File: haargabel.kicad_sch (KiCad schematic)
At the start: 42 parts, among them J1 USB_B_Micro, J2 Conn_01x03, J3 SWD, SW1 SKRKAEE020, SW2 SKRKAEE020, U1 MCP73831-2-OT, U2 ATSAMD21G18A-M, U3 TPS22929D, U4 TPS79330-EP, U5 MPU-6050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

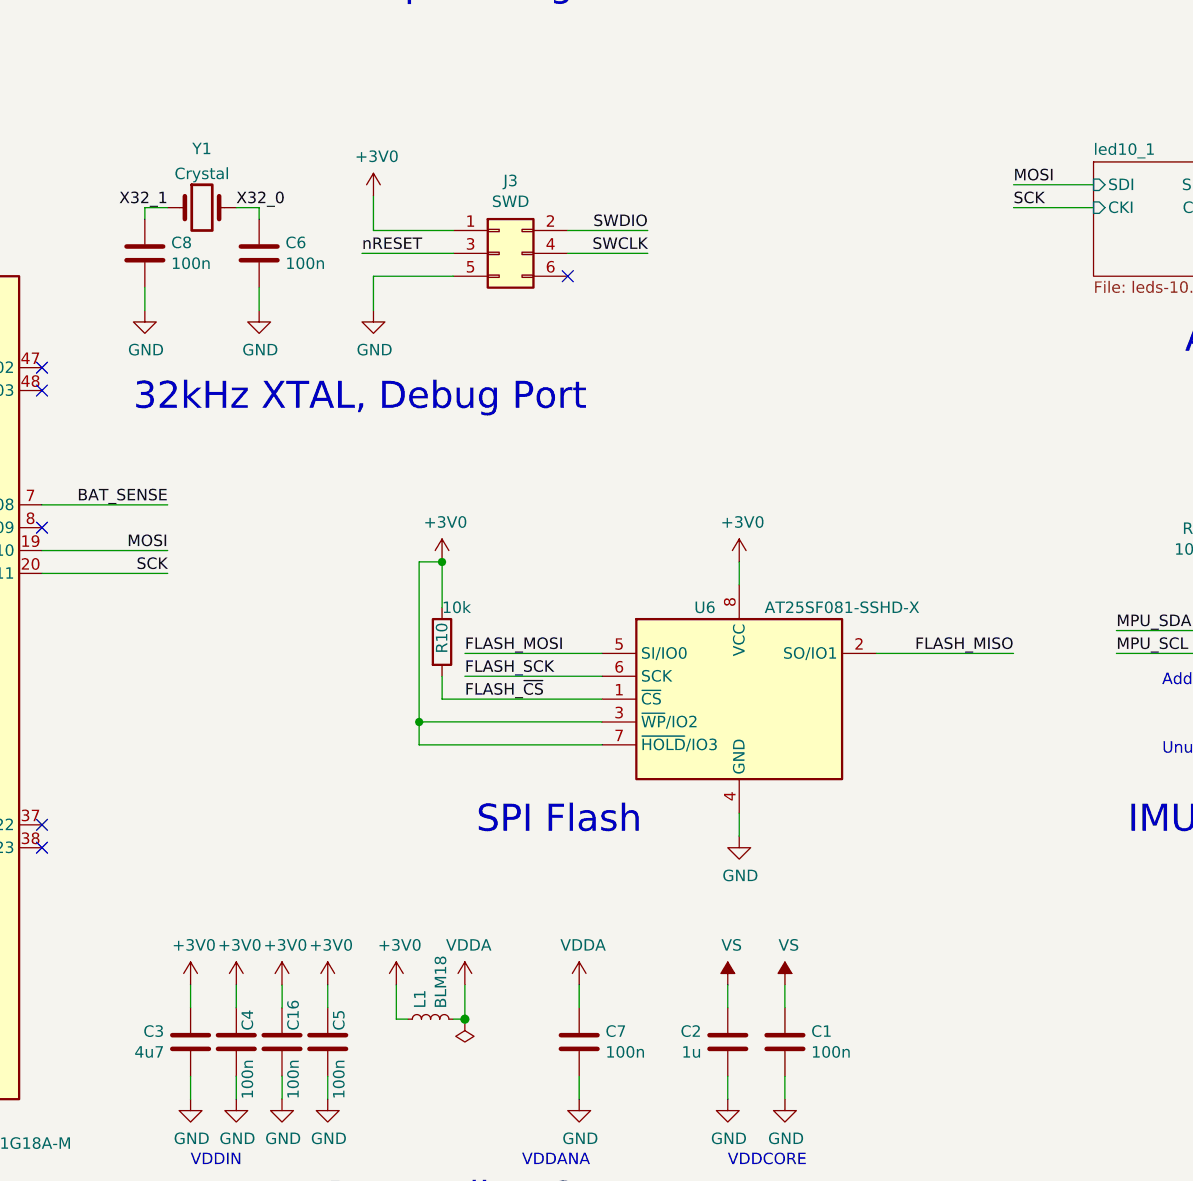
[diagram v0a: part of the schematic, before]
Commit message: Convert to KiCad7, add iBOM
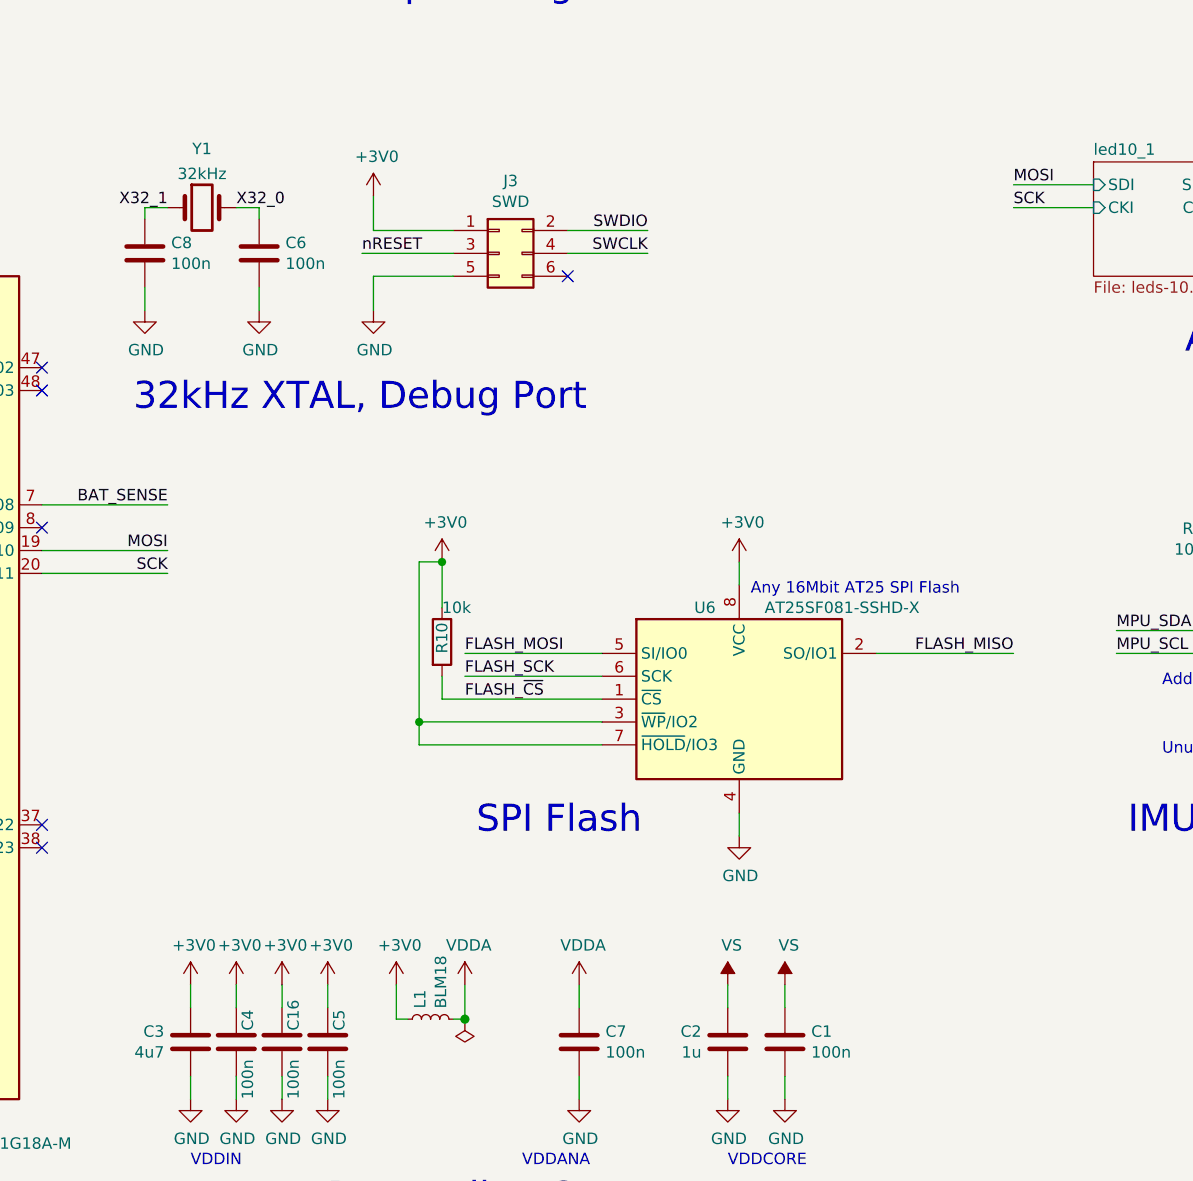
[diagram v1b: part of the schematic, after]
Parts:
- Y1: value Crystal -> 32kHz
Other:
- note added: "Any 16Mbit AT25 SPI Flash"

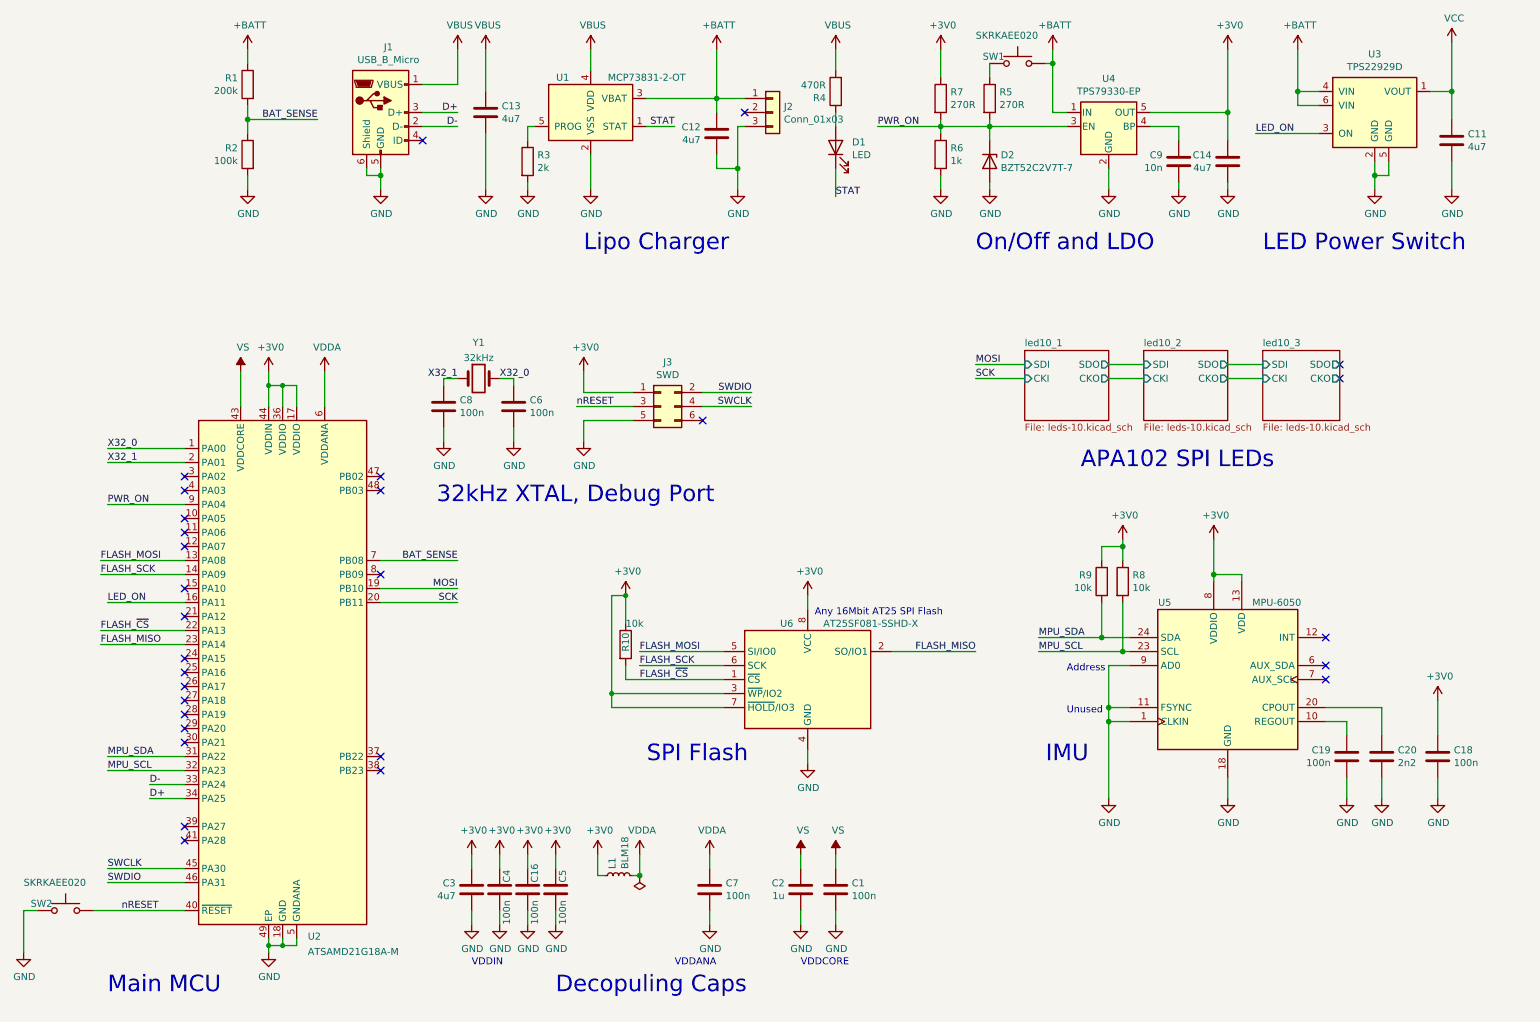
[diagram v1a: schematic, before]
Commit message: Simplify component values
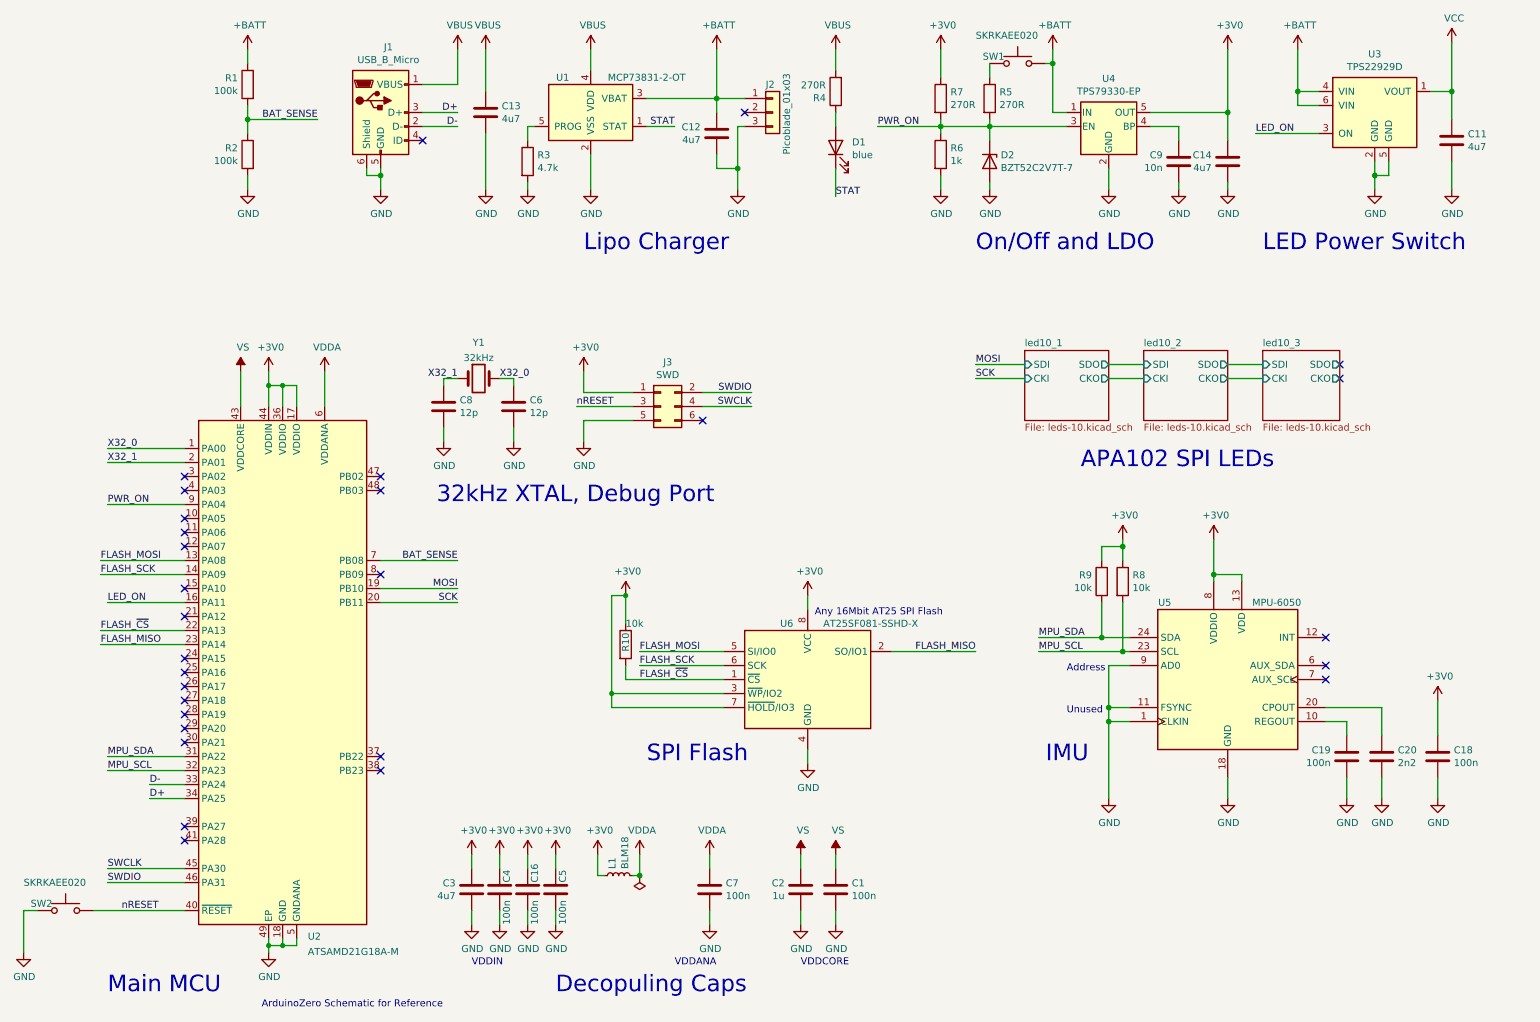
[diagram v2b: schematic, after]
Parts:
- C6, C8: value 100n -> 12p
- D1: value LED -> blue
- J2: value Conn_01x03 -> Picoblade_01x03
- R1: value 200k -> 100k
- R3: value 2k -> 4.7k
- R4: value 470R -> 270R
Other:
- note added: "ArduinoZero Schematic for Reference"
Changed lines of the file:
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@@
     (effects (font (size 3 3)) (justify left bottom))
+  )
+  (text "ArduinoZero Schematic for Reference" (at 60.96 195.58 0)
+    (effects (font (size 1.27 1.27)) (justify left bottom) (href "https://content.arduino.cc/assets/ArduinoZeroV4.0_sch.pdf"))
   )
   (text "Lipo Charger" (at 119.38 58.42 0)
@@
       (effects (font (size 1.27 1.27)) (justify left))
     )
-    (property "Value" "2k" (at 110.998 43.053 0)
+    (property "Value" "4.7k" (at 110.998 43.053 0)
       (effects (font (size 1.27 1.27)) (justify left))
     )
@@
       (effects (font (size 1.27 1.27)) (justify right))
     )
-    (property "Value" "LED" (at 168.0718 40.7162 90)
+    (property "Value" "blue" (at 168.0718 40.7162 90)
       (effects (font (size 1.27 1.27)) (justify right))
     )
@@
       (effects (font (size 1.27 1.27)) (justify left))
     )
-    (property "Value" "470R" (at 163.322 28.067 0)
+    (property "Value" "270R" (at 163.322 28.067 0)
       (effects (font (size 1.27 1.27)) (justify left))
     )
@@
       (effects (font (size 1.27 1.27)) (justify left))
     )
-    (property "Value" "200k" (at 56.642 29.083 0)
+    (property "Value" "100k" (at 56.642 29.083 0)
       (effects (font (size 1.27 1.27)) (justify left))
     )
@@
   (symbol (lib_id "Connector_Generic:Conn_01x03") (at 153.67 33.02 0) (unit 1)
     (in_bom yes) (on_board yes) (dnp no)
-    (property "Reference" "J2" (at 155.702 31.9532 0)
-      (effects (font (size 1.27 1.27)) (justify left))
-    )
-    (property "Value" "Conn_01x03" (at 155.702 34.2646 0)
+    (property "Reference" "J2" (at 152.4 27.94 0)
+      (effects (font (size 1.27 1.27)) (justify left))
+    )
+    (property "Value" "Picoblade_01x03" (at 156.21 40.64 90)
       (effects (font (size 1.27 1.27)) (justify left))
     )
@@
       (effects (font (size 1.27 1.27)) (justify left))
     )
-    (property "Value" "100n" (at 109.601 87.503 0)
+    (property "Value" "12p" (at 109.601 87.503 0)
       (effects (font (size 1.27 1.27)) (justify left))
     )
@@
       (effects (font (size 1.27 1.27)) (justify left))
     )
-    (property "Value" "100n" (at 96.901 87.503 0)
-      (effects (font (size 1.27 1.27)) (justify left))
-    )
+    (property "Value" "12p" (at 96.901 87.503 0)
+      (effects (font (size 1.27 1.27)) (justify left))
+    )
